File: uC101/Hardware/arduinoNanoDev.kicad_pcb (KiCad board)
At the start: 2 copper layers, 29 parts, among them J1 FTDI (Serial), J2 SPI Header, J3 I2C Header, J4 SAO_Conn, SW1 SW_Push, SW2 Rotary_Encoder_Switch, SW3 SW_Push

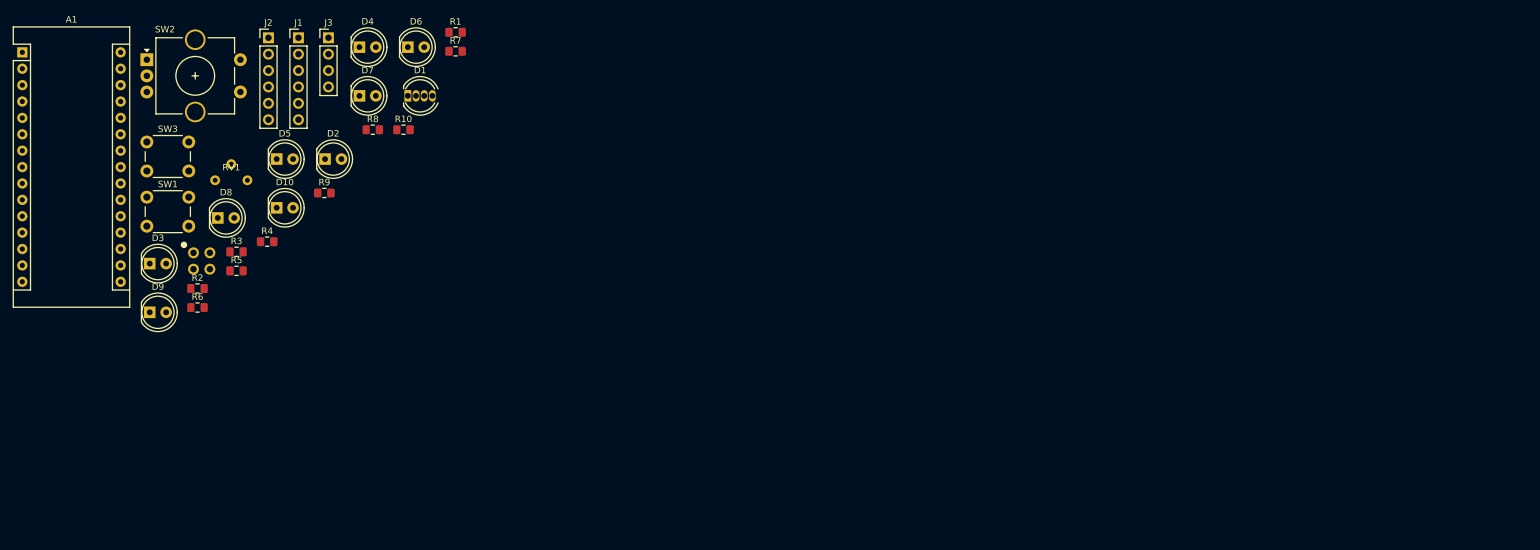
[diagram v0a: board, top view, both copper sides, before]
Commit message: Prelim route of uC101 board
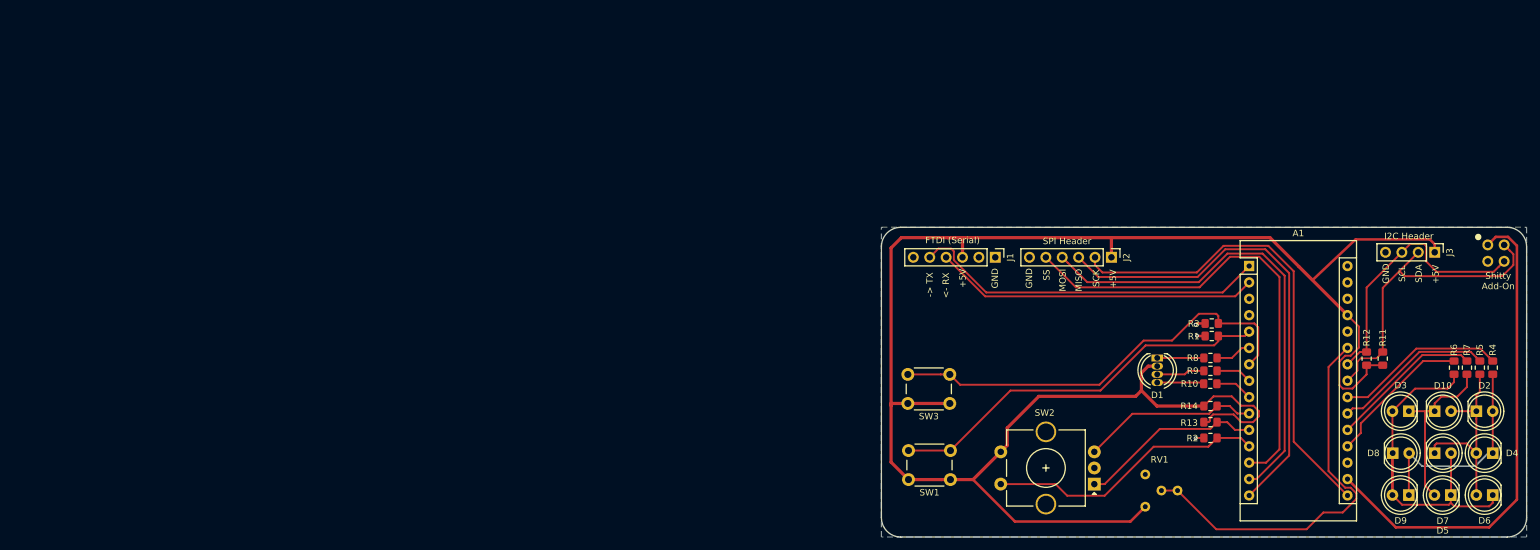
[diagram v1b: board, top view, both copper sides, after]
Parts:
- added R11: 4K7, Resistor_SMD:R_0805_2012Metric_Pad1.15x1.40mm_HandSolder, F.Cu at (240.7, 75.3)
- added R12: 4K7, Resistor_SMD:R_0805_2012Metric_Pad1.15x1.40mm_HandSolder, F.Cu at (238.2, 75.3)
- added R13: 10K, Resistor_SMD:R_0805_2012Metric_Pad1.15x1.40mm_HandSolder, F.Cu at (214.0, 85.2)
- added R14: 10K, Resistor_SMD:R_0805_2012Metric_Pad1.15x1.40mm_HandSolder, F.Cu at (214.0, 82.7)
- moved J4 200.6 mm to (258.2, 59.0)
- moved D9 197.2 mm to (244.8, 96.5), turned to 180 degrees
- moved D3 196.5 mm to (244.8, 83.5), turned to 180 degrees
- moved R6 195.0 mm to (251.8, 76.8), turned to 90 degrees
- moved R5 193.3 mm to (255.8, 76.8), turned to 90 degrees
- moved A1 193.0 mm to (220.0, 61.0)
- moved R4 190.9 mm to (257.8, 76.8), turned to 90 degrees
- moved D5 189.3 mm to (251.2, 96.5), turned to 180 degrees
- moved D4 186.6 mm to (257.8, 90.0), turned to 180 degrees
- moved D8 185.7 mm to (242.2, 90.0)
- moved D2 182.7 mm to (255.2, 83.5)
- moved D10 182.2 mm to (248.8, 83.5)
- moved D6 181.9 mm to (257.8, 96.5), turned to 180 degrees
- moved D7 175.6 mm to (248.8, 90.0)
- moved J3 174.6 mm to (248.8, 58.9), turned to 270 degrees
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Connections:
- A1 pad 10: /ENCODER_A -> /ENCODER_B
- A1 pad 11: /ENCODER_B -> /ENCODER_A
- A1 pad 17: (no net) -> +3V3
- A1 pad 19: /CHARILE_1 -> /CHARILE_3
- A1 pad 20: /CHARILE_2 -> /CHARILE_4
- A1 pad 21: /CHARILE_3 -> /CHARILE_2
- A1 pad 22: /CHARILE_4 -> /CHARILE_1
- J2 pad 2: /SS -> /SCK
- J2 pad 3: /MOSI -> /MISO
- J2 pad 4: /MISO -> /MOSI
- J2 pad 5: /SCK -> /SS
- J4 pad 1: +5V -> +3V3
- R10 pad 2: (no net) -> Net-(D1-Pad4)
- R9 pad 2: (no net) -> Net-(D1-Pad3)
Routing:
- net +5V: track 0.00 -> 290.9 mm
- net +3V3: track 0.00 -> 76.1 mm
- net /MISO: track 0.00 -> 74.2 mm
- net /SCK: track 0.00 -> 74.0 mm
- net /MOSI: track 0.00 -> 73.8 mm
- net /SS: track 0.00 -> 73.7 mm
- net /BUTTON_2: track 0.00 -> 67.4 mm
- net /POT: track 0.00 -> 61.5 mm
- net /BUTTON_1: track 0.00 -> 60.9 mm
- net Net-(D3-Pad2): track 0.00 -> 57.8 mm
- net /TX: track 0.00 -> 55.4 mm
- net /RX: track 0.00 -> 50.4 mm
- net /SDA: track 0.00 -> 48.3 mm
- net /ENCODER_SW: track 0.00 -> 43.7 mm
- net /SCL: track 0.00 -> 41.7 mm
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- added copper zone on B.Cu, net GND
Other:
- board outline added: 100 x 48 mm
- rule solder_mask_min_width: 0.25 -> 0.1
- board text added: "+5V"
- board text added: "-> TX"
- board text added: "<- RX"
- board text added: "GND"
- board text added: "MISO"
- board text added: "MOSI"
- board text added: "SCK"
- board text added: "SCL"
- board text added: "SDA"
- board text added: "SS"
- board text added: "Shitty Add-On"

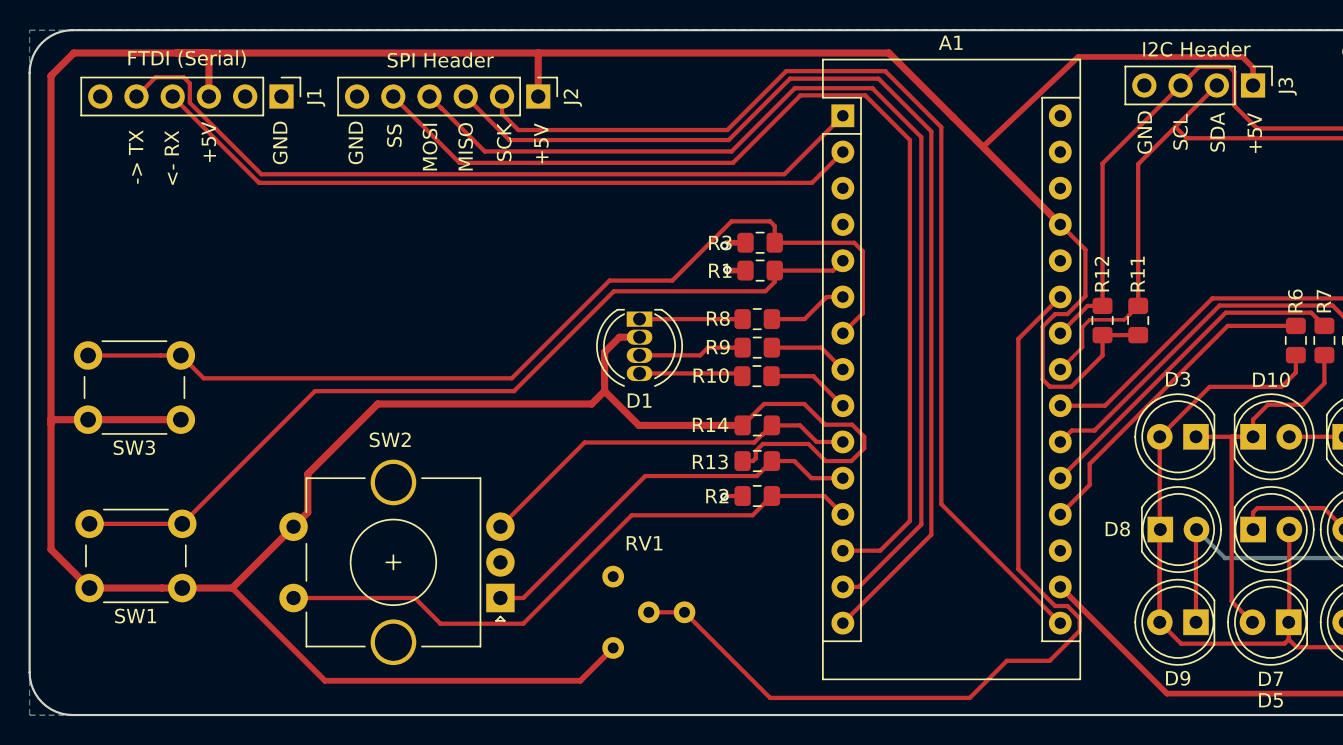
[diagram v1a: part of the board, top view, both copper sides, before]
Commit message: added more slides and resources, small routing changes
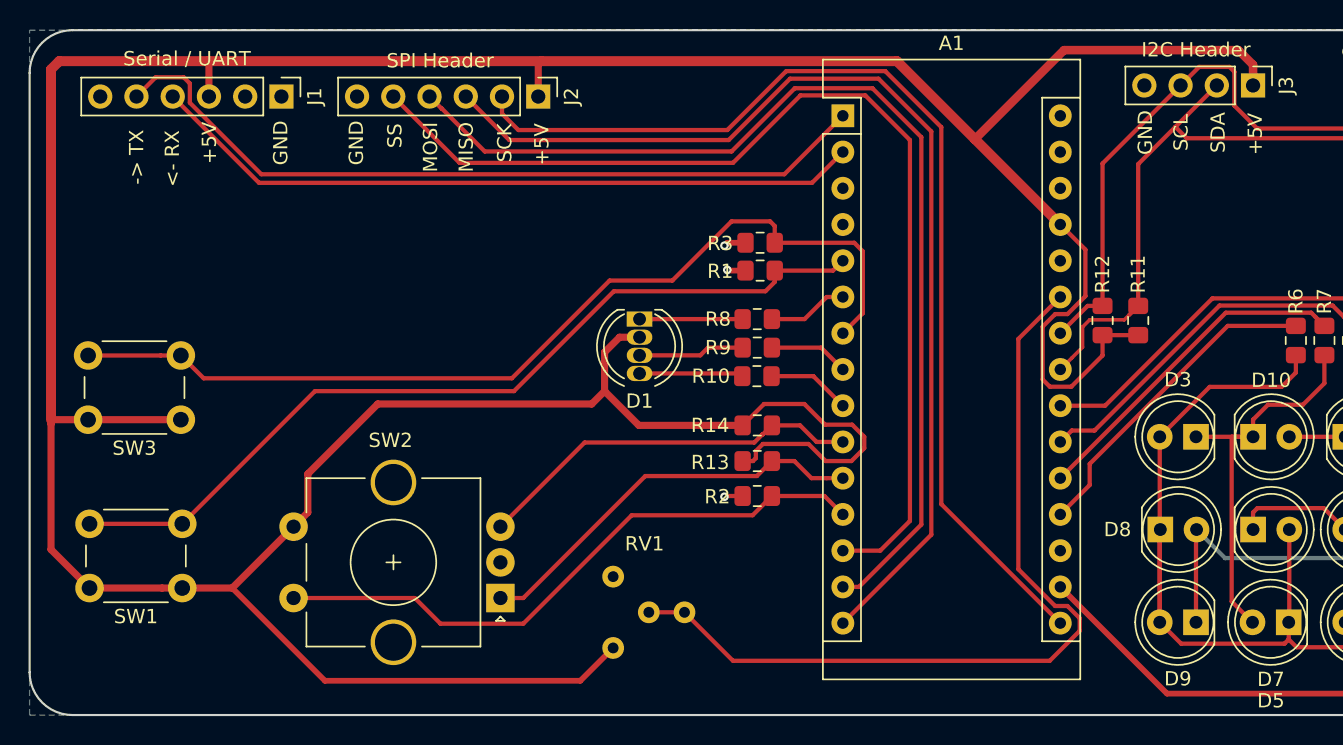
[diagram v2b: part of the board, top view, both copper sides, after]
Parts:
- J1: value FTDI (Serial) -> Serial / UART
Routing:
- net +5V: track 290.9 -> 285.0 mm
- net /POT: track 61.5 -> 59.4 mm
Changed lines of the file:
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@@
     (thickness 1.6)
     (drawings 23)
-    (tracks 291)
+    (tracks 289)
     (zones 0)
     (modules 33)
@@
   )
   (setup
-    (last_trace_width 0.3)
+    (last_trace_width 0.25)
     (user_trace_width 0.25)
     (user_trace_width 0.3)
@@
     )
     (model "${KIPRJMOD}/Libraries/3dModels.3dshapes/arduino nano.STEP"
-      (offset (xyz 15.25 -35.55 2.5))
-      (scale (xyz 1 1 1))
-      (rotate (xyz 90 -180 90))
+      (offset (xyz 0 -0 2.5))
+      (scale (xyz 1 1 1))
+      (rotate (xyz 90 -180 -90))
     )
   )
@@
       (effects (font (size 1 1) (thickness 0.15)))
     )
-    (fp_text value "FTDI (Serial)" (at -2.65 6.62) (layer F.SilkS)
+    (fp_text value "Serial / UART" (at -2.65 6.62) (layer F.SilkS)
       (effects (font (size 1 1) (thickness 0.15)))
     )
@@
   (segment (start 217.93 79.25) (end 220 81.32) (width 0.3) (layer F.Cu) (net 14))
   (segment (start 215 79.25) (end 217.93 79.25) (width 0.3) (layer F.Cu) (net 14))
-  (segment (start 234.876997 95.358999) (end 232.3 92.782002) (width 0.3) (layer F.Cu) (net 15))
-  (segment (start 235.741001 95.358999) (end 234.876997 95.358999) (width 0.3) (layer F.Cu) (net 15))
-  (segment (start 236.6 96.217998) (end 235.741001 95.358999) (width 0.3) (layer F.Cu) (net 15))
-  (segment (start 214.9 101.8) (end 228.9 101.8) (width 0.3) (layer F.Cu) (net 15))
-  (segment (start 232.3 76.64) (end 235.24 73.7) (width 0.3) (layer F.Cu) (net 15))
-  (segment (start 208.9 95.8) (end 214.9 101.8) (width 0.3) (layer F.Cu) (net 15))
+  (segment (start 208.9 95.8) (end 206.4 95.8) (width 0.3) (layer F.Cu) (net 15))
   (segment (start 232.3 92.782002) (end 232.3 76.64) (width 0.3) (layer F.Cu) (net 15))
-  (segment (start 231.5 99.2) (end 234.5 99.2) (width 0.3) (layer F.Cu) (net 15))
-  (segment (start 228.9 101.8) (end 231.5 99.2) (width 0.3) (layer F.Cu) (net 15))
+  (segment (start 208.9 95.8) (end 212.3 99.2) (width 0.3) (layer F.Cu) (net 15))
+  (segment (start 212.3 99.2) (end 234.5 99.2) (width 0.3) (layer F.Cu) (net 15))
   (segment (start 234.5 99.2) (end 236.6 97.1) (width 0.3) (layer F.Cu) (net 15))
   (segment (start 236.6 97.1) (end 236.6 96.217998) (width 0.3) (layer F.Cu) (net 15))
-  (segment (start 208.9 95.8) (end 206.4 95.8) (width 0.3) (layer F.Cu) (net 15))
+  (segment (start 234.876997 95.358999) (end 232.3 92.782002) (width 0.3) (layer F.Cu) (net 15))
+  (segment (start 236.6 96.217998) (end 235.741001 95.358999) (width 0.3) (layer F.Cu) (net 15))
+  (segment (start 232.3 76.64) (end 235.24 73.7) (width 0.3) (layer F.Cu) (net 15))
+  (segment (start 235.741001 95.358999) (end 234.876997 95.358999) (width 0.3) (layer F.Cu) (net 15))
   (segment (start 197.6 94.8) (end 196 94.8) (width 0.3) (layer F.Cu) (net 16))
   (segment (start 206.14999 86.25001) (end 197.6 94.8) (width 0.3) (layer F.Cu) (net 16))
@@
   (segment (start 173.7 94.1) (end 172.285787 94.1) (width 0.5) (layer F.Cu) (net 18))
   (segment (start 167.2 94.1) (end 164.5 91.4) (width 0.5) (layer F.Cu) (net 18))
-  (segment (start 164.5 58.2) (end 166.1 56.6) (width 0.5) (layer F.Cu) (net 18))
   (segment (start 173.6 82.3) (end 167.1 82.3) (width 0.5) (layer F.Cu) (net 18))
   (segment (start 164.5 91.4) (end 164.5 82.6) (width 0.5) (layer F.Cu) (net 18))
-  (segment (start 164.5 82.6) (end 164.5 58.2) (width 0.5) (layer F.Cu) (net 18))
   (segment (start 164.5 82.3) (end 164.5 82.6) (width 0.5) (layer F.Cu) (net 18))
   (segment (start 167.1 82.3) (end 164.5 82.3) (width 0.5) (layer F.Cu) (net 18))
-  (segment (start 166.1 56.6) (end 173.3 56.6) (width 0.5) (layer F.Cu) (net 18))
-  (segment (start 175.57 56.6) (end 175.57 59.65) (width 0.5) (layer F.Cu) (net 18))
-  (segment (start 173.3 56.6) (end 175.57 56.6) (width 0.5) (layer F.Cu) (net 18))
-  (segment (start 198.65 56.6) (end 173.3 56.6) (width 0.5) (layer F.Cu) (net 18))
-  (segment (start 198.65 59.65) (end 198.65 56.6) (width 0.5) (layer F.Cu) (net 18))
   (segment (start 235.24 68.614282) (end 235.24 68.62) (width 0.5) (layer F.Cu) (net 18))
-  (segment (start 198.65 56.6) (end 223.225718 56.6) (width 0.5) (layer F.Cu) (net 18))
-  (segment (start 223.225718 56.6) (end 227.712859 61.087141) (width 0.5) (layer F.Cu) (net 18))
-  (segment (start 227.712859 61.087141) (end 235.24 68.614282) (width 0.5) (layer F.Cu) (net 18))
-  (segment (start 248 56.875) (end 236.5 56.875) (width 0.4) (layer F.Cu) (net 18))
-  (segment (start 248.75 58.875) (end 248.75 57.625) (width 0.4) (layer F.Cu) (net 18))
-  (segment (start 248.75 57.625) (end 248 56.875) (width 0.4) (layer F.Cu) (net 18))
   (segment (start 238.2 76.375) (end 240.7 76.375) (width 0.3) (layer F.Cu) (net 18))
   (segment (start 240.725 76.375) (end 240.7 76.375) (width 0.3) (layer F.Cu) (net 18))
@@
   (segment (start 202.4 81.2) (end 203.3 80.3) (width 0.5) (layer F.Cu) (net 18))
   (segment (start 187.4 81.2) (end 202.4 81.2) (width 0.5) (layer F.Cu) (net 18))
-  (segment (start 229.812859 63.187141) (end 227.712859 61.087141) (width 0.4) (layer F.Cu) (net 18))
-  (segment (start 236.5 56.875) (end 229.812859 63.187141) (width 0.4) (layer F.Cu) (net 18))
+  (segment (start 164.5 57.75) (end 164.5 82.3) (width 0.7) (layer F.Cu) (net 18))
+  (segment (start 165.080042 57.169958) (end 164.5 57.75) (width 0.7) (layer F.Cu) (net 18))
+  (segment (start 175.555042 57.169958) (end 165.080042 57.169958) (width 0.7) (layer F.Cu) (net 18))
+  (segment (start 175.57 57.184916) (end 175.555042 57.169958) (width 0.5) (layer F.Cu) (net 18))
+  (segment (start 175.57 59.65) (end 175.57 57.184916) (width 0.5) (layer F.Cu) (net 18))
+  (segment (start 198.65 57.389916) (end 198.869958 57.169958) (width 0.5) (layer F.Cu) (net 18))
+  (segment (start 198.65 59.65) (end 198.65 57.389916) (width 0.5) (layer F.Cu) (net 18))
+  (segment (start 198.869958 57.169958) (end 175.555042 57.169958) (width 0.7) (layer F.Cu) (net 18))
+  (segment (start 223.789958 57.169958) (end 198.869958 57.169958) (width 0.7) (layer F.Cu) (net 18))
+  (segment (start 229.26 62.64) (end 235.5 56.4) (width 0.6) (layer F.Cu) (net 18))
+  (segment (start 229.26 62.64) (end 223.789958 57.169958) (width 0.7) (layer F.Cu) (net 18))
+  (segment (start 235.24 68.62) (end 229.26 62.64) (width 0.7) (layer F.Cu) (net 18))
+  (segment (start 248.75 57.425) (end 248.75 58.875) (width 0.6) (layer F.Cu) (net 18))
+  (segment (start 247.725 56.4) (end 248.75 57.425) (width 0.6) (layer F.Cu) (net 18))
+  (segment (start 235.5 56.4) (end 247.725 56.4) (width 0.6) (layer F.Cu) (net 18))
   (segment (start 220.06 88.94) (end 220 88.94) (width 0.3) (layer F.Cu) (net 19))
   (segment (start 220 88.94) (end 220 89.1) (width 0.3) (layer F.Cu) (net 19))

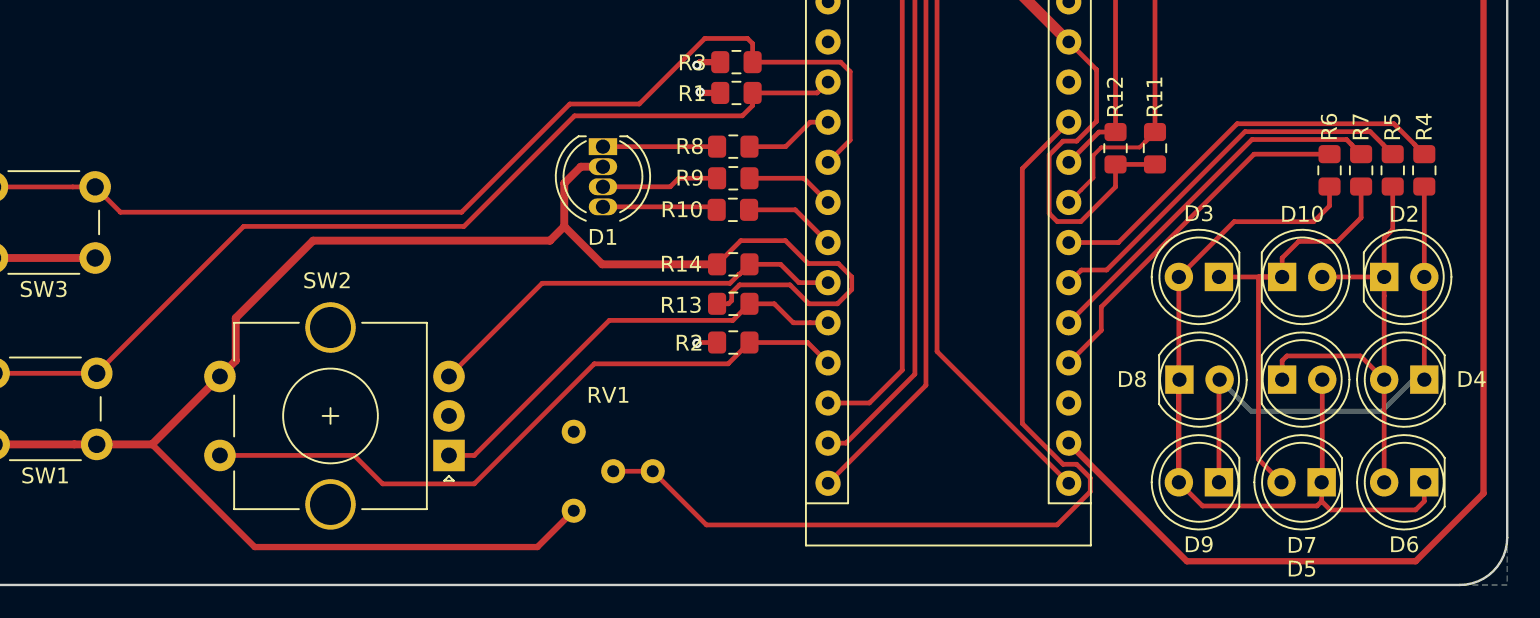
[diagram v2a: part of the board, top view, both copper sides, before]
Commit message: added test points to uC101 board
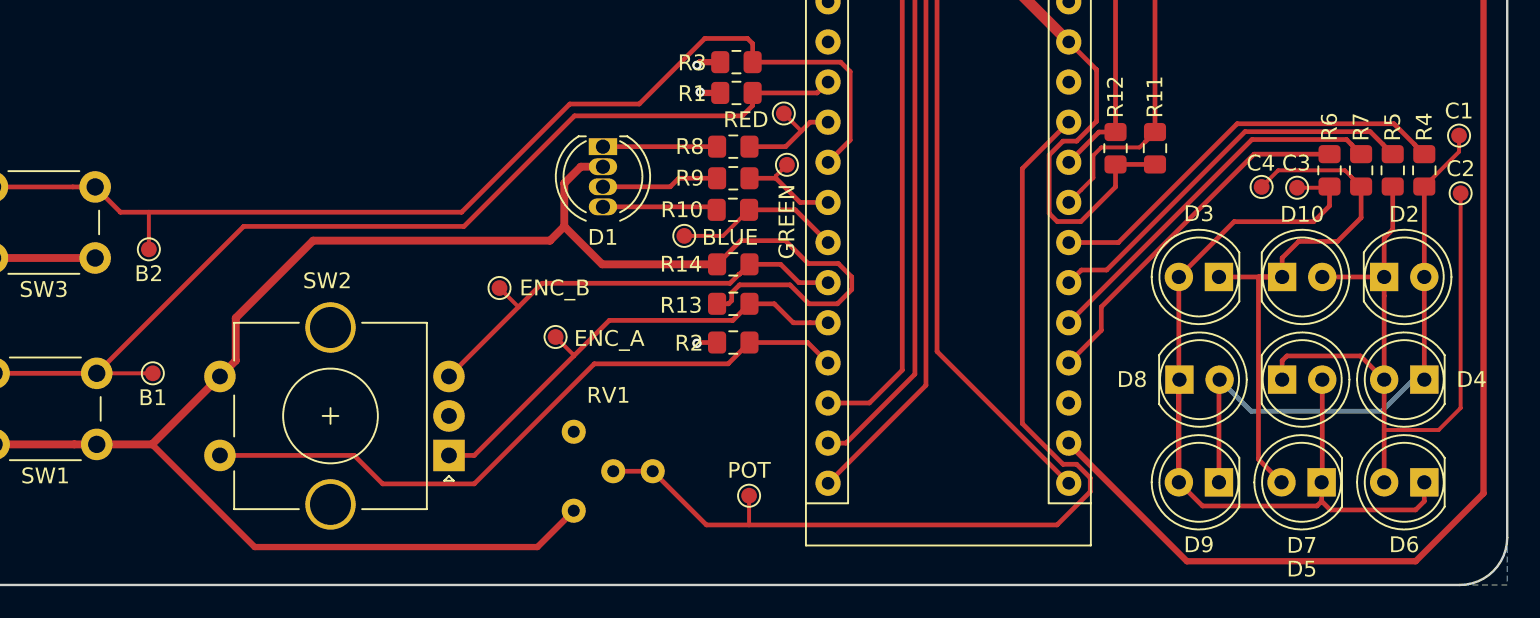
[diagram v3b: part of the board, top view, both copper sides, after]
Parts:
- added TP1: ENC_B, TestPoint:TestPoint_Pad_D1.0mm, F.Cu at (199.2, 84.2)
- added TP10: BLUE, TestPoint:TestPoint_Pad_D1.0mm, F.Cu at (210.9, 80.9)
- added TP11: GREEN, TestPoint:TestPoint_Pad_D1.0mm, F.Cu at (217.4, 76.4)
- added TP12: POT, TestPoint:TestPoint_Pad_D1.0mm, F.Cu at (215.0, 97.3)
- added TP2: B1, TestPoint:TestPoint_Pad_D1.0mm, F.Cu at (177.2, 89.6)
- added TP3: ENC_A, TestPoint:TestPoint_Pad_D1.0mm, F.Cu at (202.8, 87.3)
- added TP4: B2, TestPoint:TestPoint_Pad_D1.0mm, F.Cu at (177.0, 81.8)
- added TP5: C1, TestPoint:TestPoint_Pad_D1.0mm, F.Cu at (259.9, 74.5)
- added TP6: C2, TestPoint:TestPoint_Pad_D1.0mm, F.Cu at (260.1, 78.2)
- added TP7: C3, TestPoint:TestPoint_Pad_D1.0mm, F.Cu at (249.7, 77.8)
- added TP8: C4, TestPoint:TestPoint_Pad_D1.0mm, F.Cu at (247.4, 77.8)
- added TP9: RED, TestPoint:TestPoint_Pad_D1.0mm, F.Cu at (217.2, 73.2)
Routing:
- net Net-(D10-Pad2): track 31.3 -> 50.3 mm
- net Net-(D10-Pad1): track 28.3 -> 35.5 mm
- net /LED_BLUE: track 5.86 -> 10.6 mm
- net Net-(D2-Pad2): track 33.4 -> 37.5 mm
- net /BUTTON_1: track 60.9 -> 64.5 mm
- net /BUTTON_2: track 67.4 -> 69.7 mm
- net Net-(D3-Pad2): track 57.8 -> 59.9 mm
- net /POT: track 59.4 -> 61.2 mm
- net /ENCODER_A: track 28.5 -> 30.2 mm
- net /ENCODER_B: track 27.4 -> 29.1 mm
- net /LED_RED: track 5.62 -> 7.19 mm
- net /LED_GREEN: track 5.61 -> 6.75 mm
